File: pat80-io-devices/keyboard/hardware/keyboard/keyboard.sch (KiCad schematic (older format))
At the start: 94 parts

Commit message: WIP Keyboard schematics
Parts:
- removed D? (x10): 1N4148, symbol Device:D
- removed SW? (x10): Q, symbol Switch:SW_Push
- added D? (x5): 1N4148, symbol Device:D
- added SW?: DELETE, symbol Switch:SW_Push
- added SW?: ', symbol Switch:SW_Push
- added SW?: SPACE, symbol Switch:SW_Push
- added SW?: PATO, symbol Switch:SW_Push
- added SW?: SHIFT, symbol Switch:SW_Push
- SW?: value Q -> E
- SW?: value Q -> T
- SW?: value Q -> U
- SW?: value Q -> O
- SW?: value Q -> D
- SW?: value Q -> G
- SW?: value Q -> J
- SW?: value Q -> L
- SW?: value Q -> C
- SW?: value Q -> B
- SW?: value Q -> M
- SW?: value Q -> .
- SW?: value Q -> V
- SW?: value Q -> N
- SW?: value Q -> ,
- SW?: value Q -> -
- SW?: value Q -> F
- SW?: value Q -> H
- SW?: value Q -> K
- SW?: value Q -> RETURN
- SW?: value Q -> R
- SW?: value Q -> Y
- SW?: value Q -> I
- SW?: value Q -> DELETE
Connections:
- wire segments 187 -> 172
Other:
- moved on the sheet: R?

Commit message: Completed keyboard schematics
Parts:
- removed J?: Conn_01x10, symbol Connector_Generic:Conn_01x10
- removed R?: 10k, symbol Device:R
- added C?: 56pF, symbol Device:C
- added D? (x29): 1N4148, symbol Device:D
- added J? (x2): Keyboard connector, symbol Connector_Generic:Conn_02x17_Odd_Even
- added R?: 10k, symbol Device:R
- added SW?: 0, symbol Switch:SW_Push
- added SW?: 8, symbol Switch:SW_Push
- added SW?: 6, symbol Switch:SW_Push
- added SW?: 4, symbol Switch:SW_Push
- added SW?: 2, symbol Switch:SW_Push
- added SW? (x16): NC, symbol Switch:SW_Push
- added SW?: PATO, symbol Switch:SW_Push
- added SW?: CONTROL, symbol Switch:SW_Push
- added SW?: SHIFT, symbol Switch:SW_Push
- added SW?: À, symbol Switch:SW_Push
- added SW?: RETURN, symbol Switch:SW_Push
- added SW?: È, symbol Switch:SW_Push
- added SW?: DEL, symbol Switch:SW_Push
- added SW?: ', symbol Switch:SW_Push
- SW?: value Q -> 1
- SW?: value E -> 3
- SW?: value T -> 5
- SW?: value U -> 7
- SW?: value O -> 9
- SW?: value A -> Q
- SW?: value D -> E
- SW?: value G -> T
- SW?: value J -> U
- SW?: value L -> O
- SW?: value Z -> A
- SW?: value C -> D
- SW?: value B -> G
- SW?: value M -> J
- SW?: value . -> L
- SW?: value X -> Z
- SW?: value V -> C
- SW?: value N -> B
- SW?: value , -> M
- SW?: value - -> .
- SW?: value S -> X
- SW?: value F -> V
- SW?: value H -> N
- SW?: value K -> ,
- SW?: value RETURN -> -
- SW?: value DELETE -> P
- SW?: value ' -> I
- SW?: value SPACE -> Y
- SW?: value PATO -> R
- SW?: value SHIFT -> W
- SW?: value W -> S
- SW?: value R -> F
- SW?: value Y -> H
- SW?: value I -> K
- SW?: value DELETE -> Ò
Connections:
- net labels added: MTXVCC
- wire segments 172 -> 272
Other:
- note added: "Keyboard controller"
- note added: "Keyboard matrix"
- note added: "PAT80 Keyboard"
- note added: "PCB Ground plane"
- note added: "Pull-up resistors"
- note added: "Smoothing cap\n"
- note added: "The PAT80 keyboard is seen from the computer as a readonly block of 64 bytes of memory\nin the I/O space mapped to the first 3 of the 5 I/O address available for every single I/O device.\n\nThe keyboard controller is a board plugged on the I/O backplane and connected to the matrix board with a\n34-pin female-to-female flat ribbon cable (e.g. the ones used by IBM PC floppy disk drives)"
- moved on the sheet: C?, D?, IOBUS, R?, SW?, U?

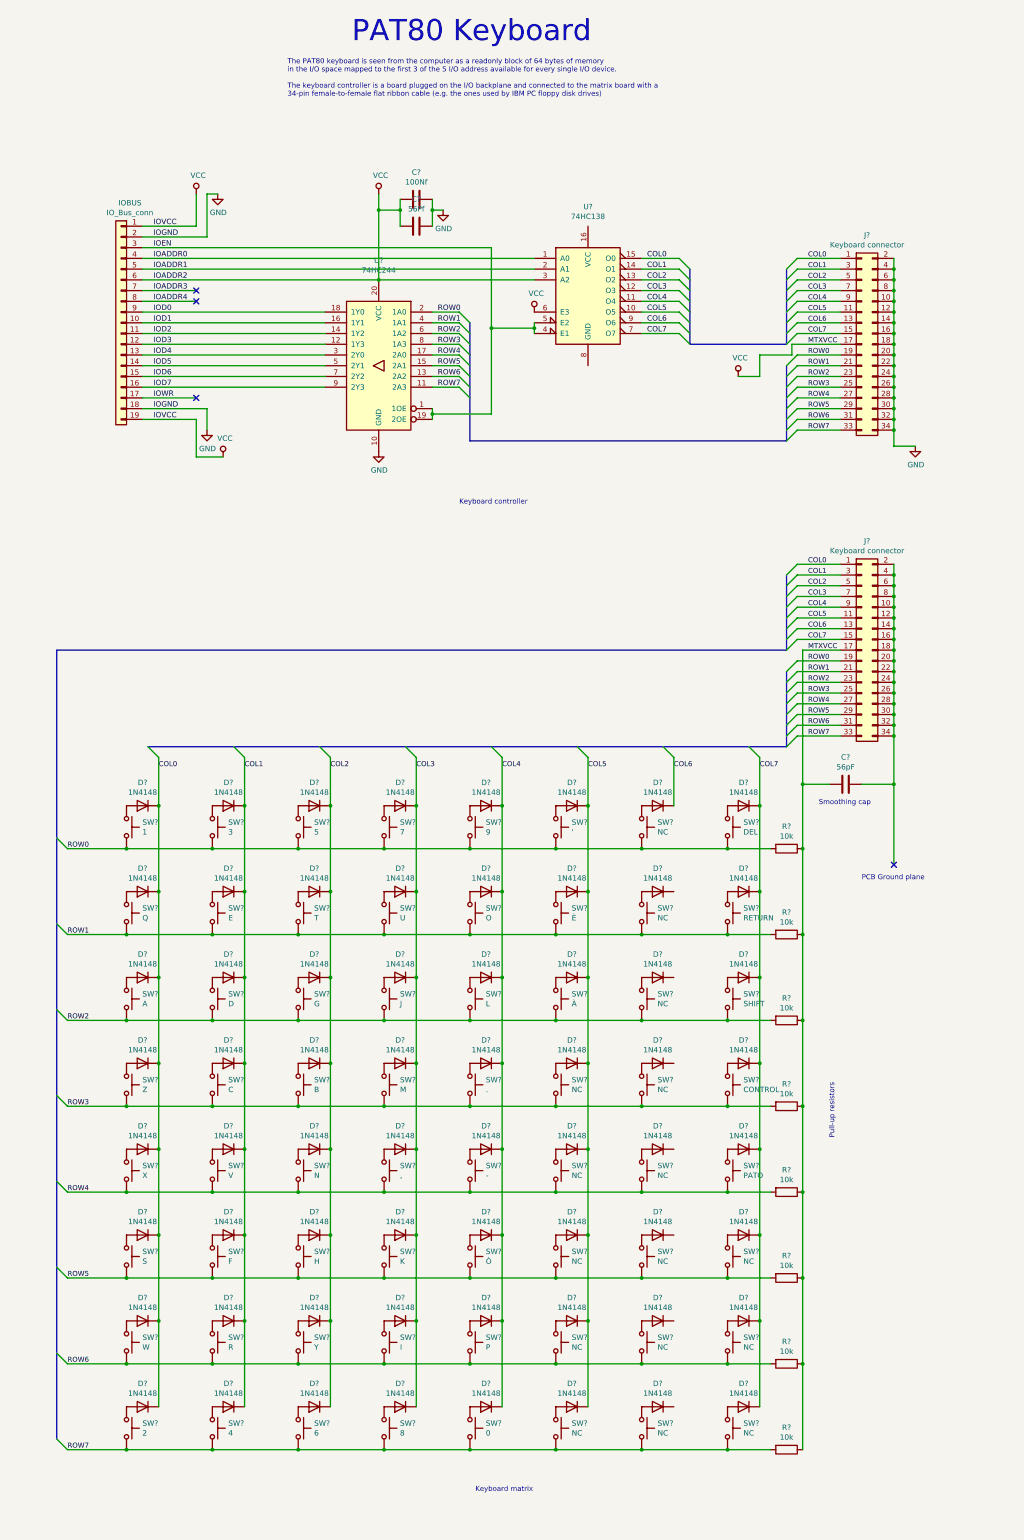
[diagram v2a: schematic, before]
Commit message: Final keyboard schematics with joystick port
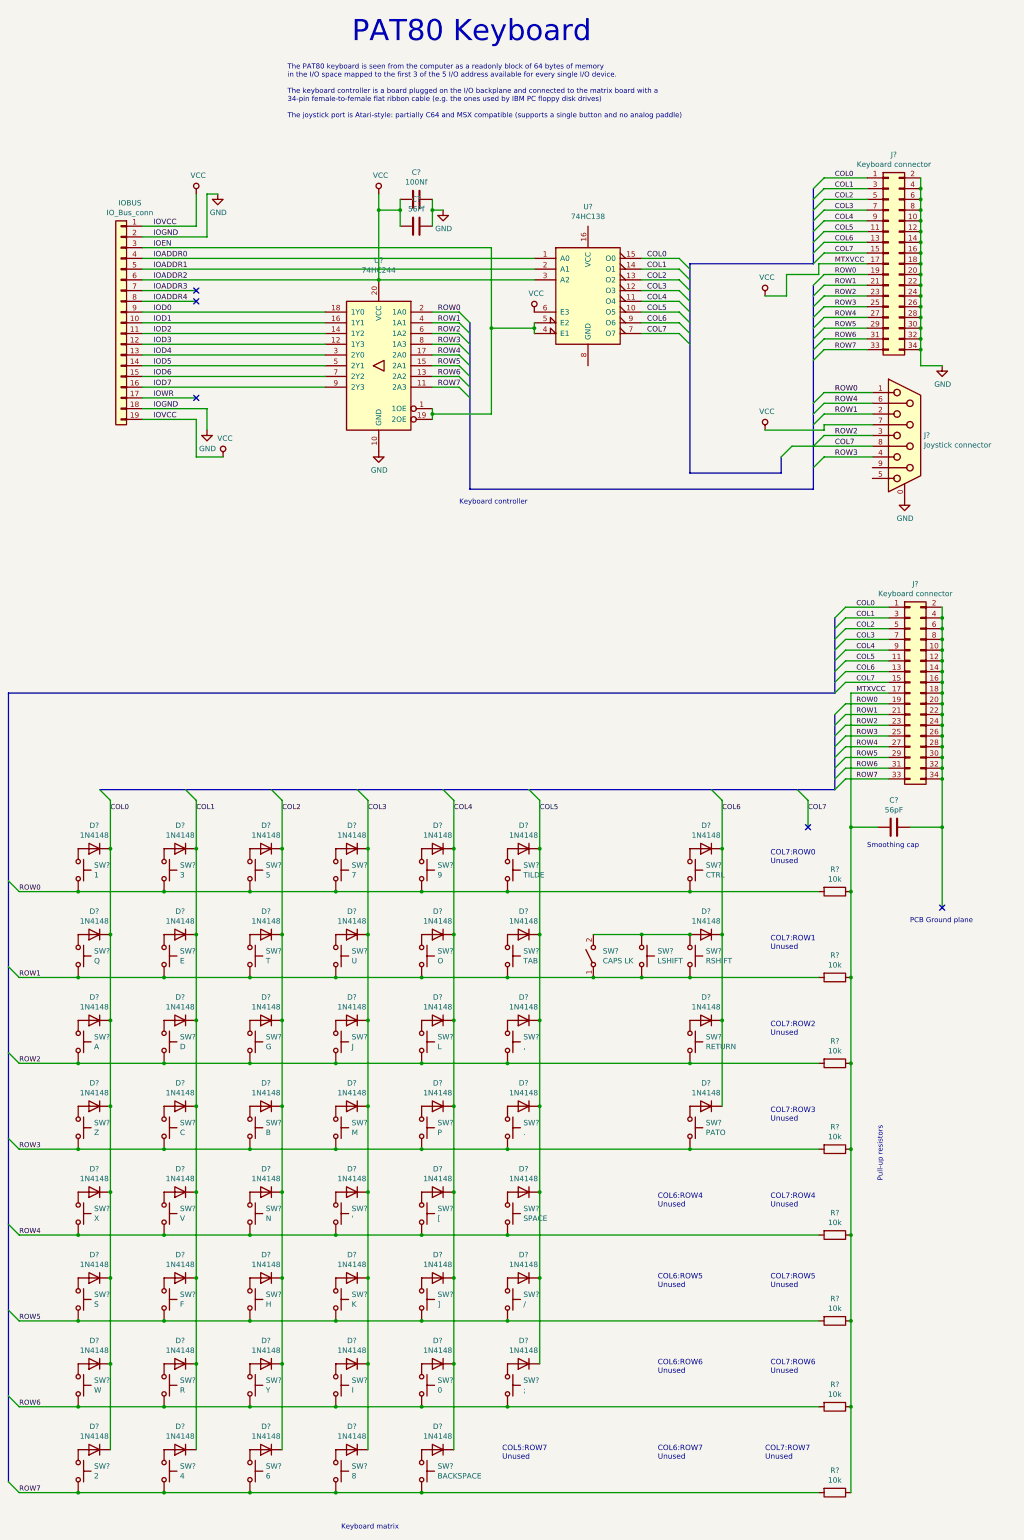
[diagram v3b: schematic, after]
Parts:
- removed D? (x13): 1N4148, symbol Device:D
- removed SW? (x8): NC, symbol Switch:SW_Push
- removed SW?: PATO, symbol Switch:SW_Push
- removed SW?: CONTROL, symbol Switch:SW_Push
- removed SW?: SHIFT, symbol Switch:SW_Push
- removed SW?: RETURN, symbol Switch:SW_Push
- removed SW?: DEL, symbol Switch:SW_Push
- added J?: Joystick connector, symbol Connector:DB9_Female_MountingHoles
- added SW?: LSHIFT, symbol Switch:SW_Push
- added SW?: CAPS LK, symbol Switch:SW_SPST
- SW?: value 0 -> BACKSPACE
- SW?: value . -> P
- SW?: value , -> '
- SW?: value - -> [
- SW?: value P -> 0
- SW?: value Ò -> ]
- SW?: value NC -> /
- SW?: value NC -> SPACE
- SW?: value NC -> PATO
- SW?: value NC -> .
- SW?: value NC -> RETURN
- SW?: value À -> ,
- SW?: value NC -> RSHIFT
- SW?: value È -> TAB
- SW?: value NC -> CTRL
- SW?: value ' -> TILDE
- SW?: value NC -> ;
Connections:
- net COL6: now also D?.1 (K), D?.1 (K), D?.1 (K)
- net COL7: now also J?.8
- net GND: now also J?.0 (PAD)
- net ROW0: now also J?.1
- net ROW1: now also J?.2, SW?.1 (A), SW?.2
- net ROW2: now also J?.3
- net ROW3: now also J?.4
- net ROW4: now also J?.6
- net VCC: now also J?.7
- net at D?.2 (A), SW?.1: now also SW?.1, SW?.2 (B)
- no-connect marks 4 -> 5
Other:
- note added: "COL5:ROW7\nUnused"
- note added: "COL6:ROW4\nUnused"
- note added: "COL6:ROW5\nUnused"
- note added: "COL6:ROW6\nUnused"
- note added: "COL6:ROW7\nUnused"
- note added: "COL7:ROW0\nUnused"
- note added: "COL7:ROW1\nUnused"
- note added: "COL7:ROW2\nUnused"
- note added: "COL7:ROW3\nUnused"
- note added: "COL7:ROW4\nUnused"
- note added: "COL7:ROW5\nUnused"
- note added: "COL7:ROW6\nUnused"
- note added: "COL7:ROW7\nUnused"
- note added: "The PAT80 keyboard is seen from the computer as a readonly block of 64 bytes of memory\nin the I/O space mapped to the first 3 of the 5 I/O address available for every single I/O device.\n\nThe keyboard controller is a board plugged on the I/O backplane and connected to the matrix board with a\n34-pin female-to-female flat ribbon cable (e.g. the ones used by IBM PC floppy disk drives)\n\nThe joys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"
- note removed: "The PAT80 keyboard is seen from the computer as a readonly block of 64 bytes of memory\nin the I/O space mapped to the first 3 of the 5 I/O address available for every single I/O device.\n\nThe keyboard controller is a board plugged on the I/O backplane and connected to the matrix board with a\n34-pin female-to-female flat ribbon cable (e.g. the ones used by IBM PC floppy disk drives)"
- moved on the sheet: C?, D?, J?, R?, SW?

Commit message: Assigning footprints
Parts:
- removed SW?: CAPS LK, symbol Switch:SW_SPST
- added C3: 100Nf, Capacitor_THT:CP_Radial_Tantal_D6.0mm_P5.00mm, symbol Device:C
- added C4: 56Pf, Capacitor_THT:CP_Radial_Tantal_D6.0mm_P5.00mm, symbol Device:C
- added D9: CAPSLOCK_LED, LED_THT:LED_D5.0mm, symbol Device:LED
- added R1: 470, Resistor_THT:R_Axial_DIN0207_L6.3mm_D2.5mm_P7.62mm_Horizontal, symbol Device:R
- added SW9: CAPSLOCK_SW, symbol Switch:SW_DPST
- C1, C2, C5: renamed from C?; footprint (none) -> Capacitor_THT:CP_Radial_Tantal_D6.0mm_P5.00mm
- D1, D10, D11, D12, D13, D14, D15, D16, D17, D18, D19, D2, D20, D21, D22, D23, D24, D25, D26, D27, D28, D29, D3, D30, D31, D32, D33, D34, D35, D36, D37, D38, D39, D4, D40, D41, D42, D43, D44, D45, D46, D47, D48, D49, D5, D50, D51, D52, D6, D7, D8: renamed from D?; footprint (none) -> Diode_THT:D_DO-41_SOD81_P7.62mm_Horizontal
- IOBUS1: renamed from IOBUS; footprint (none) -> Connector_PinHeader_2.54mm:PinHeader_1x19_P2.54mm_Horizontal
- J1, J3: renamed from J?; footprint (none) -> Connector_PinHeader_2.54mm:PinHeader_2x17_P2.54mm_Vertical
- J2: renamed from J?; footprint (none) -> Connector_Dsub:DSUB-9_Female_Horizontal_P2.77x2.84mm_EdgePinOffset4.94mm_Housed_MountingHolesOffset7.48mm
- R2, R3, R4, R5, R6, R7, R8, R9: renamed from R?; footprint (none) -> Resistor_THT:R_Axial_DIN0207_L6.3mm_D2.5mm_P7.62mm_Horizontal
- SW1, SW10, SW11, SW12, SW13, SW14, SW15, SW16, SW17, SW18, SW19, SW2, SW20, SW21, SW22, SW23, SW24, SW25, SW26, SW27, SW28, SW29, SW3, SW30, SW31, SW32, SW33, SW34, SW35, SW36, SW37, SW38, SW39, SW4, SW40, SW42, SW44, SW45, SW47, SW48, SW5, SW6, SW7, SW8: renamed from SW?; footprint (none) -> Button_Switch_Keyboard:SW_Cherry_MX1A_1.00u_PCB
- SW41: renamed from SW?; footprint (none) -> Button_Switch_Keyboard:SW_Cherry_MX1A_2.00u_Plate
- SW43, SW50, SW53: renamed from SW?; footprint (none) -> Button_Switch_Keyboard:SW_Cherry_MX1A_1.50u_PCB
- SW46, SW52: renamed from SW?; footprint (none) -> Button_Switch_Keyboard:SW_Cherry_MX1A_2.25u_PCB
- SW49: renamed from SW?; footprint (none) -> Button_Switch_Keyboard:SW_Cherry_MX1A_1.25u_PCB
- SW51: renamed from SW?; footprint (none) -> Button_Switch_Keyboard:SW_Cherry_MX1A_1.75u_PCB
- U1: renamed from U?; footprint (none) -> Package_DIP:DIP-20_W7.62mm_LongPads
- U2: renamed from U?; footprint (none) -> Package_DIP:DIP-16_W7.62mm_LongPads
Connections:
- net GND: now also U2.8 (GND), C3.1, C4.1, SW9.4
- net VCC: now also U2.16 (VCC), C3.2, C4.2, R1.1
- net CL_ASSY_COL: now reaches D50.2 (A), SW49.1, SW51.1
- net CL_ASSY_COL: now also SW9.1
- net ROW1 renamed CL_ASSY_ROW
- net CL_ASSY_ROW: now also SW9.2
- new net: D9.1 (K), SW9.3
- new net: D9.2 (A), R1.2
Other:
- note added: "Caps lock assy"
- moved on the sheet: C1, C2, C5, D1, D10, D11, D12, D13, D14, D15, D16, D17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

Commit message: Split keyboard into two different schematics: kb controller and kb assembly. Started routing keyboard pcb.
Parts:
- removed C1, C3: 100Nf, Capacitor_THT:CP_Radial_Tantal_D6.0mm_P5.00mm, symbol Device:C
- removed C2, C4: 56Pf, Capacitor_THT:CP_Radial_Tantal_D6.0mm_P5.00mm, symbol Device:C
- removed IOBUS1: IO_Bus_conn, Connector_PinHeader_2.54mm:PinHeader_1x19_P2.54mm_Horizontal, symbol Connector_Generic:Conn_01x19
- removed J1: Keyboard connector, Connector_PinHeader_2.54mm:PinHeader_2x17_P2.54mm_Vertical, symbol Connector_Generic:Conn_02x17_Odd_Even
- removed J2: Joystick connector, Connector_Dsub:DSUB-9_Female_Horizontal_P2.77x2.84mm_EdgePinOffset4.94mm_Housed_MountingHolesOffset7.48mm, symbol Connector:DB9_Female_MountingHoles
- removed SW9: CAPSLOCK_SW, symbol Switch:SW_DPST
- removed U1: 74HC244, Package_DIP:DIP-20_W7.62mm_LongPads, symbol 74xx:74HC244
- removed U2: 74HC138, Package_DIP:DIP-16_W7.62mm_LongPads, symbol 74xx:74LS138
- added SW54: CAPSLK, footprints:SW_TH_DPDT_Pushbutton_Latched, symbol Switch:SW_DPDT_x2
- added SW9: CAPSLK_LED, footprints:SW_TH_DPDT_Pushbutton_Latched, symbol Switch:SW_DPDT_x2
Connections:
- net GND: now also C5.1, J3.10 (Pin_10), J3.12 (Pin_12), J3.14 (Pin_14), J3.16 (Pin_16), J3.18 (Pin_18), J3.2 (Pin_2), J3.20 (Pin_20), J3.22 (Pin_22), J3.24 (Pin_24), J3.26 (Pin_26), J3.28 (Pin_28), J3.30 (Pin_30), J3.32 (Pin_32), J3.34 (Pin_34), J3.4 (Pin_4), J3.6 (Pin_6), J3.8 (Pin_8), SW9.5 (B)
- net at D9.1 (K): now also SW9.6 (C)
- net CL_ASSY_COL: no longer names the net of D50.2 (A), SW49.1, SW51.1
- net CL_ASSY_COL: now also SW54.3 (C)
- net CL_ASSY_ROW renamed ROW1
- net ROW1: now also SW54.2 (B)
- no-connect marks 5 -> 3
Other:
- note added: "Caps lock switch is double pole,\nthe second pole controls\nthe caps lock led"
- note removed: "Keyboard controller"
- note removed: "PCB Ground plane"
- moved on the sheet: C5, D1, D10, D11, D12, D13, D14, D15, D16, D17, D18, D19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

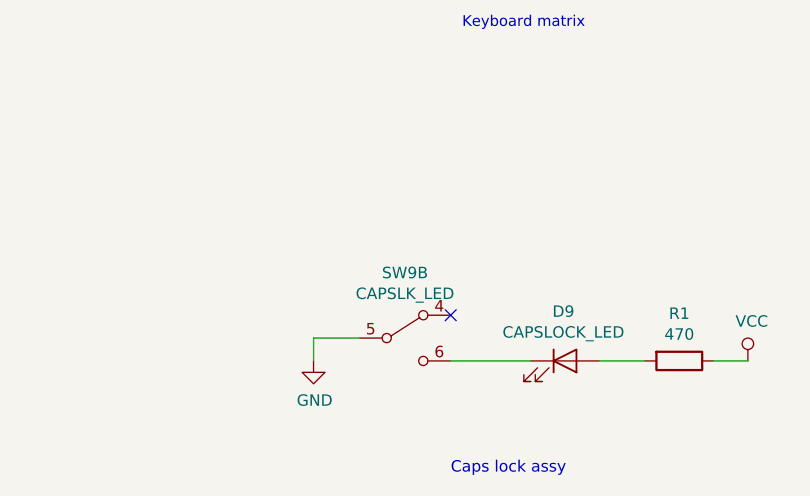
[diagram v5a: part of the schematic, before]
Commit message: Fine-positioned caps lock switch
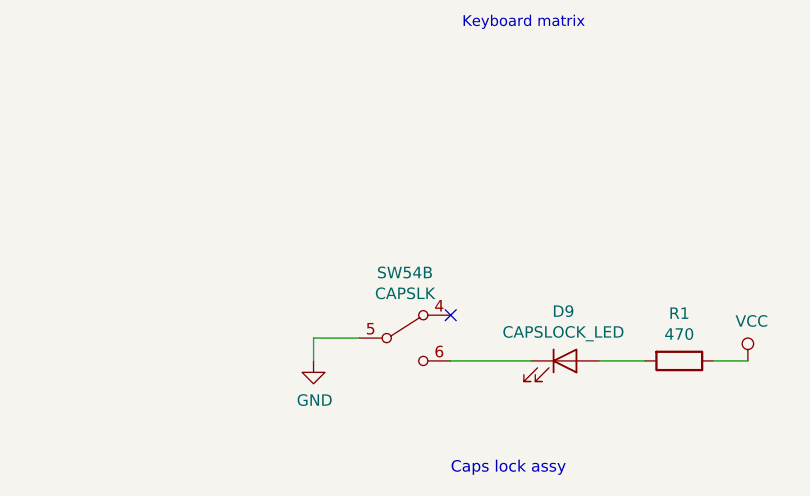
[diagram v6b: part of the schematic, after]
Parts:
- SW54: renamed from SW9; value CAPSLK_LED -> CAPSLK
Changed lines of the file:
@@
 Connection ~ 7450 6050
 $Comp
-L Switch:SW_DPDT_x2 SW9
+L Switch:SW_DPDT_x2 SW54
 U 2 1 6074126F
 P 5350 13250
-F 0 "SW9" H 5350 13535 50  0000 C CNN
-F 1 "CAPSLK_LED" H 5350 13444 50  0000 C CNN
+F 0 "SW54" H 5350 13535 50  0000 C CNN
+F 1 "CAPSLK" H 5350 13444 50  0000 C CNN
 F 2 "footprints:SW_TH_DPDT_Pushbutton_Latched" H 5350 13250 50  0001 C CNN
 F 3 "" H 5350 13250 50  0001 C CNN
@@
 Connection ~ 9400 11250
 $Comp
-L power:VCC #PWR?
+L power:VCC #PWR0101
 U 1 1 6076CE62
 P 9600 11500
-F 0 "#PWR?" H 9600 11350 50  0001 C CNN
+F 0 "#PWR0101" H 9600 11350 50  0001 C CNN
 F 1 "VCC" H 9617 11673 50  0000 C CNN
 F 2 "" H 9600 11500 50  0001 C CNN
@@
 	9400 3800 9400 3850
 $Comp
-L power:VCC #PWR?
+L power:VCC #PWR0102
 U 1 1 6078C764
 P 8800 4050
-F 0 "#PWR?" H 8800 3900 50  0001 C CNN
+F 0 "#PWR0102" H 8800 3900 50  0001 C CNN
 F 1 "VCC" H 8817 4223 50  0000 C CNN
 F 2 "" H 8800 4050 50  0001 C CNN
@@
 Connection ~ 10250 4600
 $Comp
-L power:GND #PWR?
+L power:GND #PWR0103
 U 1 1 6079E0E1
 P 10600 4600
-F 0 "#PWR?" H 10600 4350 50  0001 C CNN
+F 0 "#PWR0103" H 10600 4350 50  0001 C CNN
 F 1 "GND" H 10605 4427 50  0000 C CNN
 F 2 "" H 10600 4600 50  0001 C CNN
@@
 $EndComp
 $Comp
-L power:VCC #PWR?
+L power:VCC #PWR0104
 U 1 1 607C8BE9
 P 1850 13300
-F 0 "#PWR?" H 1850 13150 50  0001 C CNN
+F 0 "#PWR0104" H 1850 13150 50  0001 C CNN
 F 1 "VCC" H 1867 13473 50  0000 C CNN
 F 2 "" H 1850 13300 50  0001 C CNN
@@
 	1850 13300 2250 13300
 $Comp
-L power:GND #PWR?
+L power:GND #PWR0105
 U 1 1 607D1F15
 P 3100 13300
-F 0 "#PWR?" H 3100 13050 50  0001 C CNN
+F 0 "#PWR0105" H 3100 13050 50  0001 C CNN
 F 1 "GND" H 3105 13127 50  0000 C CNN
 F 2 "" H 3100 13300 50  0001 C CNN

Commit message: WIP routing keyboard
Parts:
- SW1, SW10, SW11, SW12, SW13, SW14, SW15, SW16, SW17, SW18, SW19, SW2, SW20, SW21, SW22, SW23, SW24, SW25, SW26, SW27, SW28, SW29, SW3, SW30, SW31, SW32, SW33, SW34, SW35, SW36, SW37, SW38, SW39, SW4, SW40, SW42, SW44, SW45, SW47, SW48, SW5, SW6, SW7, SW8: footprint Button_Switch_Keyboard:SW_Cherry_MX1A_1.00u_PCB -> Button_Switch_Keyboard:SW_Cherry_MX1A_1.00u_Plate
- SW43, SW50, SW53: footprint Button_Switch_Keyboard:SW_Cherry_MX1A_1.50u_PCB -> Button_Switch_Keyboard:SW_Cherry_MX1A_1.50u_Plate
- SW46, SW52: footprint Button_Switch_Keyboard:SW_Cherry_MX1A_2.25u_PCB -> Button_Switch_Keyboard:SW_Cherry_MX1A_2.25u_Plate
- SW49: footprint Button_Switch_Keyboard:SW_Cherry_MX1A_1.25u_PCB -> Button_Switch_Keyboard:SW_Cherry_MX1A_1.25u_Plate
- SW51: footprint Button_Switch_Keyboard:SW_Cherry_MX1A_1.75u_PCB -> Button_Switch_Keyboard:SW_Cherry_MX1A_1.75u_Plate
